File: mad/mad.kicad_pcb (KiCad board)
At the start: 2 copper layers, 39 x 33 mm, 25 parts, among them X1 Вилка_PLS6, X2 Вилка_PLS6, X3 Вилка_PLS6, X4 Вилка_PLS8

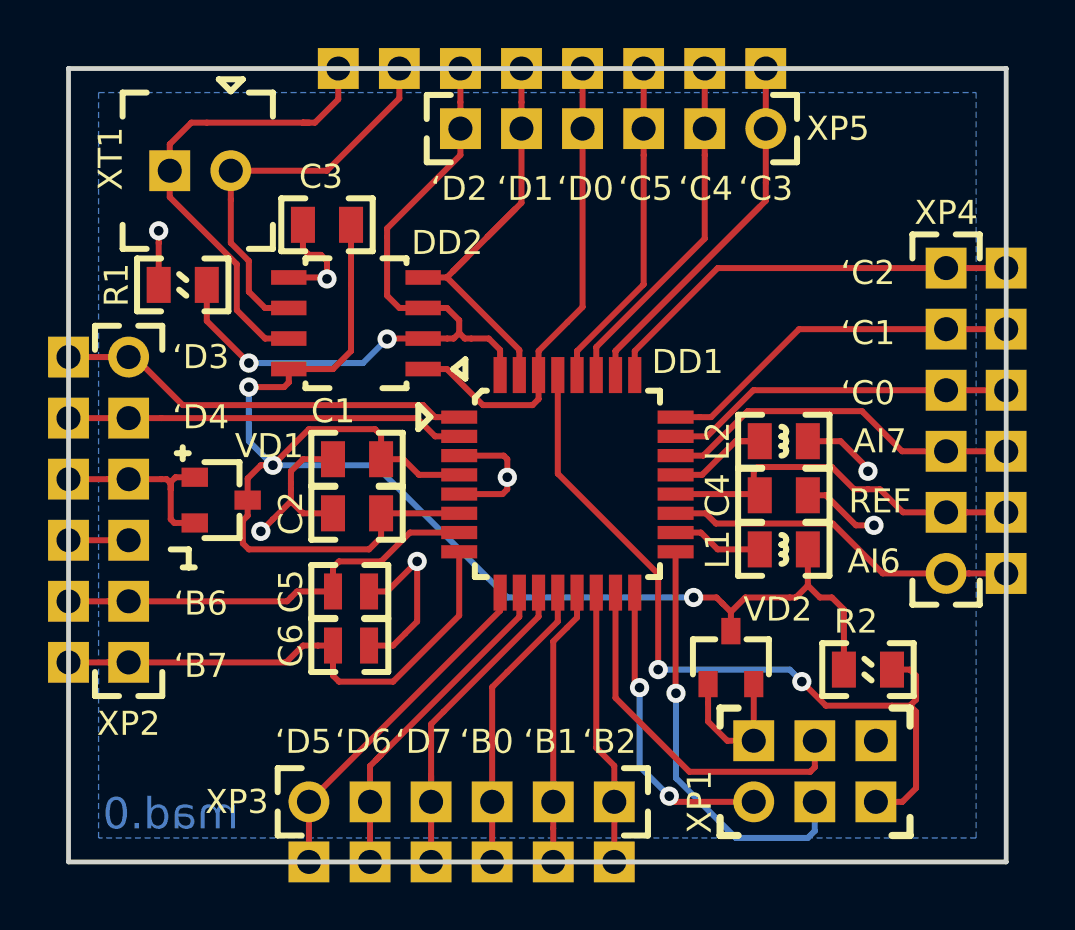
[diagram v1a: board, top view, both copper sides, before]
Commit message: начата работа над функцией прошивки модуля ввода/вывода
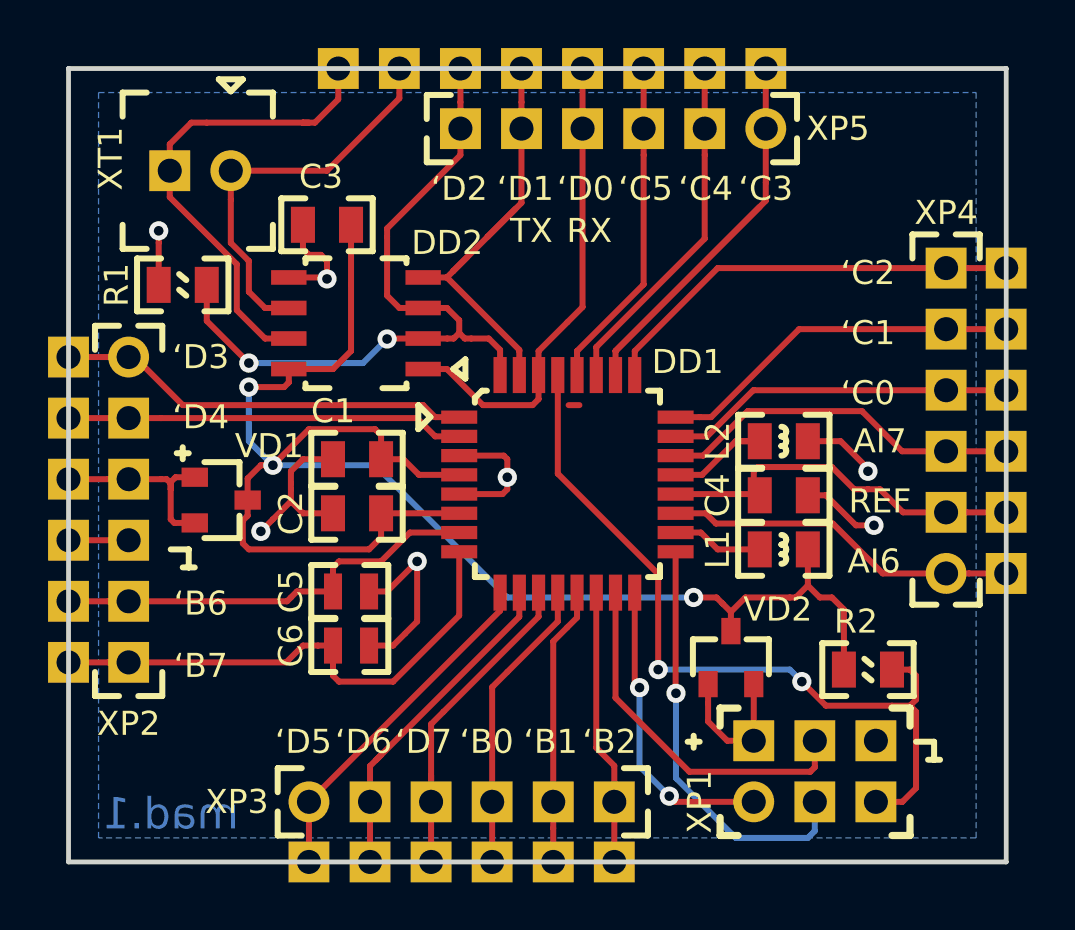
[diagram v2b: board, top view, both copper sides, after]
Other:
- board text added: "RX"
- board text added: "TX"
- board text added: "mad.1"
- board text removed: "mad.0"
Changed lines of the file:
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@@
-(kicad_pcb (version 20171130) (host pcbnew "(5.0.0-3-g5ebb6b6)")
+(kicad_pcb (version 20171130) (host pcbnew "(5.0.0)")
   (general
     (thickness 1.6)
-    (drawings 37)
-    (tracks 348)
+    (drawings 45)
+    (tracks 349)
     (zones 0)
     (modules 25)
@@
     (solder_mask_min_width 0.2)
     (aux_axis_origin 0 0)
-    (visible_elements FFFFFF7F)
+    (visible_elements 7FFFFFFF)
     (pcbplotparams
       (layerselection 0x010f0_ffffffff)
@@
       (xy -9.79055 4.523452)) (layer B.SilkS) (width 0.01))
   )
+  (gr_line (start 75.5 72) (end 76 72) (layer F.SilkS) (width 0.25))
+  (gr_line (start 75.75 71.75) (end 75.75 72.25) (layer F.SilkS) (width 0.25))
+  (gr_line (start 85 72) (end 85.75 72) (layer F.SilkS) (width 0.25))
+  (gr_line (start 85.75 72.75) (end 86 72.75) (layer F.SilkS) (width 0.25))
+  (gr_line (start 85.75 72.75) (end 85.5 72.75) (layer F.SilkS) (width 0.25))
+  (gr_line (start 85.75 72) (end 85.75 72.75) (layer F.SilkS) (width 0.25))
+  (gr_text RX (at 71.41 50.75) (layer F.SilkS)
+    (effects (font (size 1 1) (thickness 0.2)))
+  )
+  (gr_text TX (at 69 50.75) (layer F.SilkS)
+    (effects (font (size 1 1) (thickness 0.2)))
+  )
   (dimension 33 (width 0.3) (layer Eco1.User)
     (gr_text "33,000 мм" (at 40.4 60.5 270) (layer Eco1.User)
@@
     (effects (font (size 1 1) (thickness 0.2)))
   )
-  (gr_text mad.0 (at 54 75) (layer B.Cu)
+  (gr_text mad.1 (at 54 75) (layer B.Cu)
     (effects (font (size 1.3 1.3) (thickness 0.25)) (justify mirror))
   )
@@
   (gr_line (start 88.75 44) (end 88.75 77) (layer Edge.Cuts) (width 0.2))
   (gr_line (start 49.75 44) (end 88.75 44) (layer Edge.Cuts) (width 0.2))
+  (segment (start 71 58) (end 70.55001 58) (width 0.25) (layer F.Cu) (net 0))
   (segment (start 63.676998 60.25) (end 62.75 60.25) (width 0.25) (layer F.Cu) (net 1))
   (segment (start 64.326998 60.9) (end 63.676998 60.25) (width 0.25) (layer F.Cu) (net 1))
